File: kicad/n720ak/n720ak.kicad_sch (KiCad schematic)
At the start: 0 parts

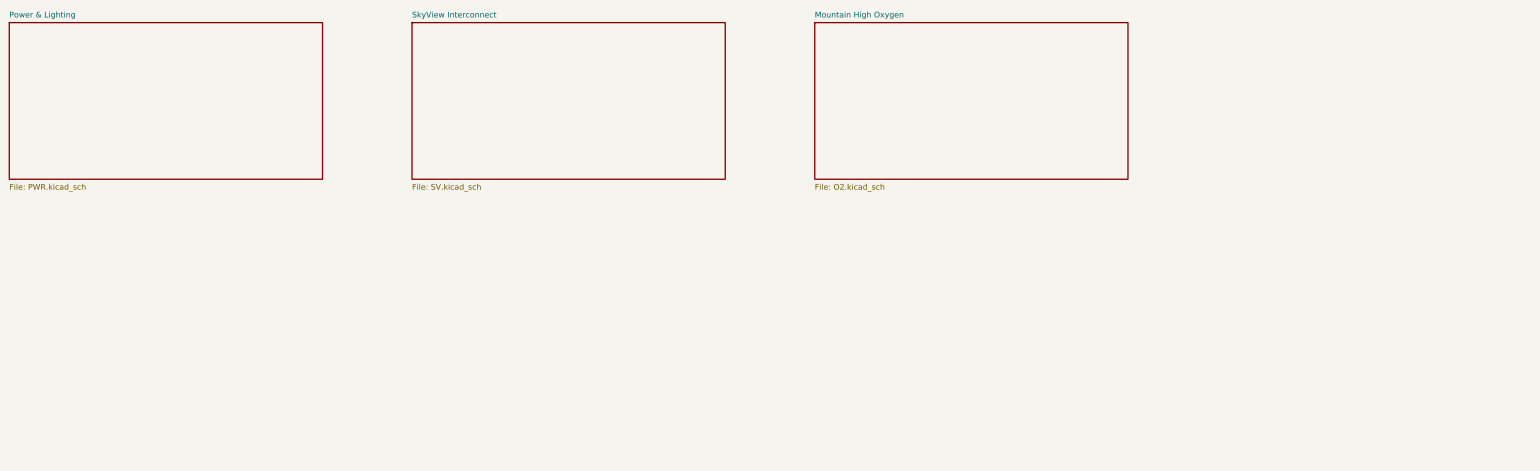
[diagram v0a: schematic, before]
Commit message: Record the owner's second round of answers; add OnSpeed and EMS sheets
24 recorded changes now, from the owner:

- OnSpeed is a Gen2v4 box on a DB-25 harness. Its pinout in sys-34 matches
  Phil's Gen2v4 aircraft harness drawing pin for pin, so the as-installed
  harness gets its own sheet: power from the essential bus through a 1 A
  blade fuse, SkyView Serial 4 TX in, right audio channel as mono into GMA
  245 Alert 3, flap position spliced into the VP-X flap sensor wire, and
  the button, LED and volume pot on a 6-conductor control cable.
- The CO detector is installed and powered. Only its audio and EMS data
  wires were cut - the audio input now carries OnSpeed and the EMS pin
  carries the MZ-30. sys-42 said it was not installed; corrected.
- EMS pin 31 is on the DB37 - the EMS's other connector has only 25 pins.
- COM 2 flip/flop has been wired to the grips since the build; the 2017
  drawing omits it. Recorded, with its return pin still to confirm.
- The GTN serial cut, OnSpeed, USB and MZ-30 work dates to about February
  2026.

Cross-sheet references follow the SteinAir convention: each sheet names
the far end as a label (ONSPEED DB25-10 on one side, GMA245 J1-29 on the
other).

sys-34 corrected: OnSpeed audio goes straight to the GMA 245, not through
the SkyView; power is from the essential bus on 1 A, not from the PFD on
2 A; the left audio channel is unused.

Five sheets, all verifying clean against their as-built wire lists.

Co-Authored-By: Claude Opus 5.5 <noreply@anthropic.com>
Claude-Session: https://claude.ai/code/session_015SpGdnvPFhutgEDurpngu2
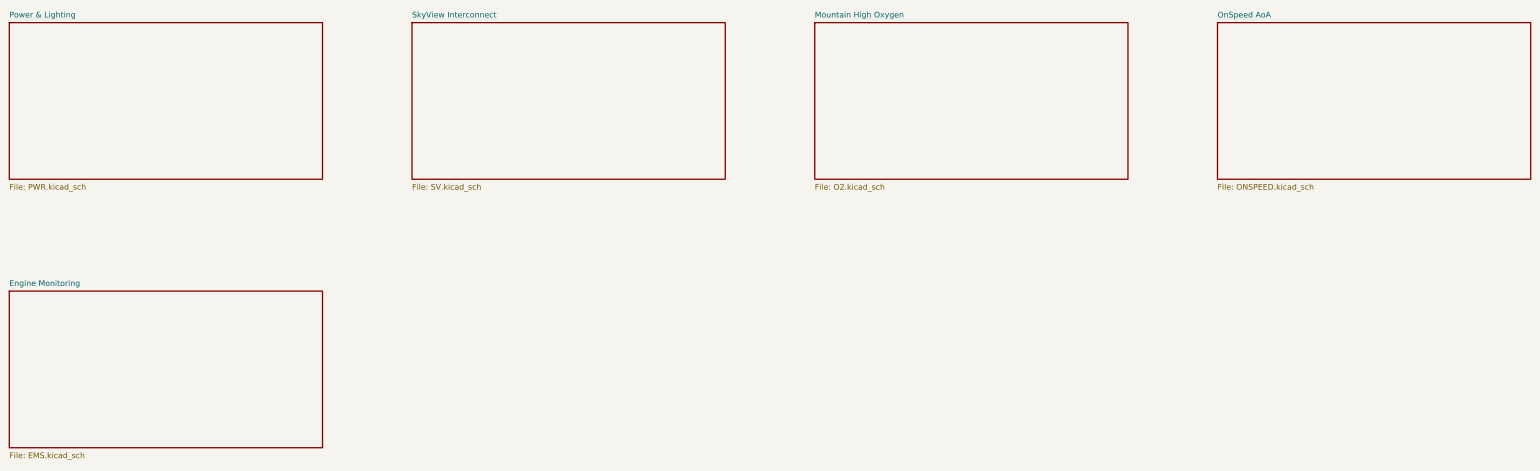
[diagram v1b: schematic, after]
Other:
- added sheet Engine Monitoring (EMS.kicad_sch)
- added sheet OnSpeed AoA (ONSPEED.kicad_sch)
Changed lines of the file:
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@@
 			(effects (font (size 1.27 1.27)) (justify left top)))
 		(instances (project "n720ak" (path "/05ae3897-9dd7-5bc2-b238-7f217081554a" (page "4")))))
+	(sheet (at 300 40) (size 70 35) (fields_autoplaced yes)
+		(stroke (width 0.1524) (type solid)) (fill (color 0 0 0 0.0000))
+		(property "Sheetname" "OnSpeed AoA" (at 300 39 0)
+			(effects (font (size 1.27 1.27)) (justify left bottom)))
+		(property "Sheetfile" "ONSPEED.kicad_sch" (at 300 76 0)
+			(effects (font (size 1.27 1.27)) (justify left top)))
+		(instances (project "n720ak" (path "/05ae3897-9dd7-5bc2-b238-7f217081554a" (page "5")))))
+	(sheet (at 30 100) (size 70 35) (fields_autoplaced yes)
+		(stroke (width 0.1524) (type solid)) (fill (color 0 0 0 0.0000))
+		(property "Sheetname" "Engine Monitoring" (at 30 99 0)
+			(effects (font (size 1.27 1.27)) (justify left bottom)))
+		(property "Sheetfile" "EMS.kicad_sch" (at 30 136 0)
+			(effects (font (size 1.27 1.27)) (justify left top)))
+		(instances (project "n720ak" (path "/05ae3897-9dd7-5bc2-b238-7f217081554a" (page "6")))))
 	(sheet_instances (path "/" (page "1")))
 )

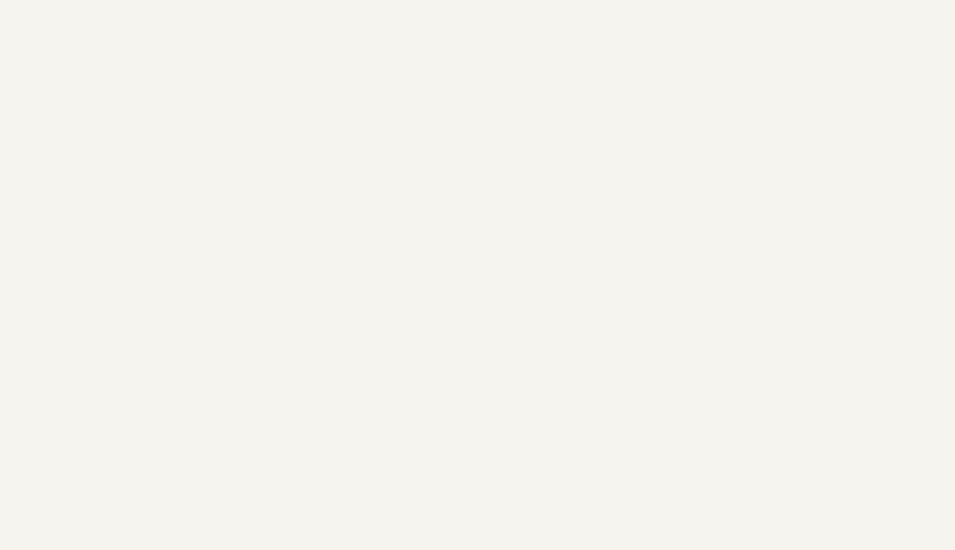
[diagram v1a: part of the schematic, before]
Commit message: Build wing, terminal-block and EMS wire lists from the handbook tables
The wings, the under-seat terminal blocks and the EMS-220's 37-pin connector
are on no SteinAir drawing. Their only record is the owner's typed build
notes in sys-24 and sys-33. scripts/wirelist_handbook.py reads those tables
directly, so the WING and EMS wire lists cannot drift from the handbook.
Every join across connectors records what it rests on: matching bundle and
colour, a function named at both ends, or a manufacturer colour code (Dynon
servo pigtail, Ray Allen trim sensor leads). A join none of those settles
is flagged with the question that would settle it.

- KiCad: new WING sheet, full EMS sheet. The project netlist is now verified
  as a whole, which proves the cross-sheet labels merge (EMS pin 10 reaches
  the roll trim sensor through TB-L 3 and wing-root pin 12)
- INSPECT.md groups rows by question and picks up "Confirm at inspection"
  notes: 14 items
- SV trim motor outputs become labels that join TB-L on the WING sheet
- changes.tsv: CO detector RMA replacement (452-101-012, Dec 2025), its EFIS
  wire on EMS 31 and that wire's removal; C011 now names MZ-30 output Molex
  pin 5, 2026-03
- sys-33: AeroSun Vx colour table corrected to the Rev C manual (blue =
  taxi, yellow = wig-wag, green = sync), which matches TB-R 3's green pair
- sys-24: EMS pins 36/37 added to the unused table

Co-Authored-By: Claude Opus 5.5 <noreply@anthropic.com>
Claude-Session: https://claude.ai/code/session_015SpGdnvPFhutgEDurpngu2
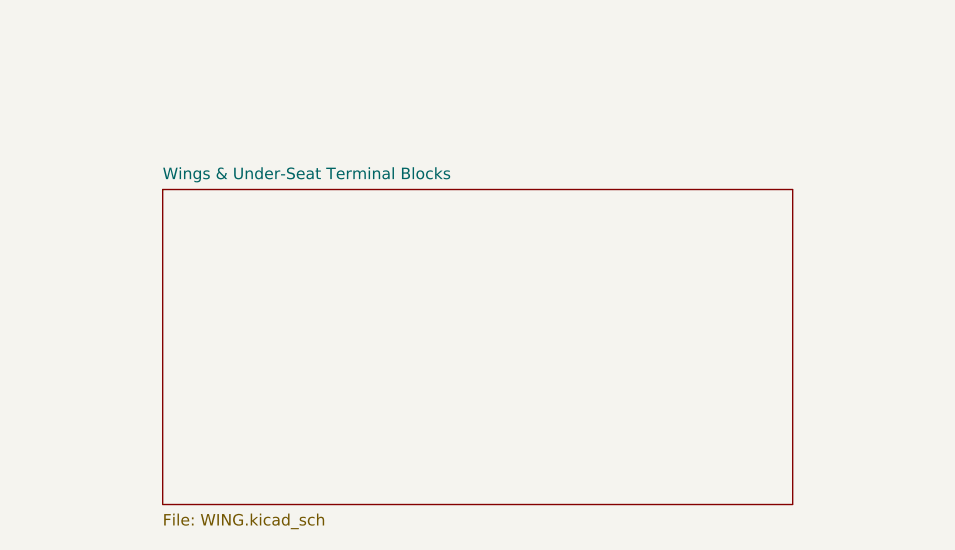
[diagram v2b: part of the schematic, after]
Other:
- added sheet Wings & Under-Seat Terminal Blocks (WING.kicad_sch)
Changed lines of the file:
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@@
 			(effects (font (size 1.27 1.27)) (justify left top)))
 		(instances (project "n720ak" (path "/05ae3897-9dd7-5bc2-b238-7f217081554a" (page "6")))))
+	(sheet (at 120 100) (size 70 35) (fields_autoplaced yes)
+		(stroke (width 0.1524) (type solid)) (fill (color 0 0 0 0.0000))
+		(property "Sheetname" "Wings & Under-Seat Terminal Blocks" (at 120 99 0)
+			(effects (font (size 1.27 1.27)) (justify left bottom)))
+		(property "Sheetfile" "WING.kicad_sch" (at 120 136 0)
+			(effects (font (size 1.27 1.27)) (justify left top)))
+		(instances (project "n720ak" (path "/05ae3897-9dd7-5bc2-b238-7f217081554a" (page "7")))))
 	(sheet_instances (path "/" (page "1")))
 )
